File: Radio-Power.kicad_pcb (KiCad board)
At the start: 2 copper layers, 52.7 x 45.7 mm, 18 parts, among them J1 Input, J2 Radio Power, Q1 BS170, Q2 FQP27P06, Q3 BS170, U1 L7805, U2 ATtiny85-20PU

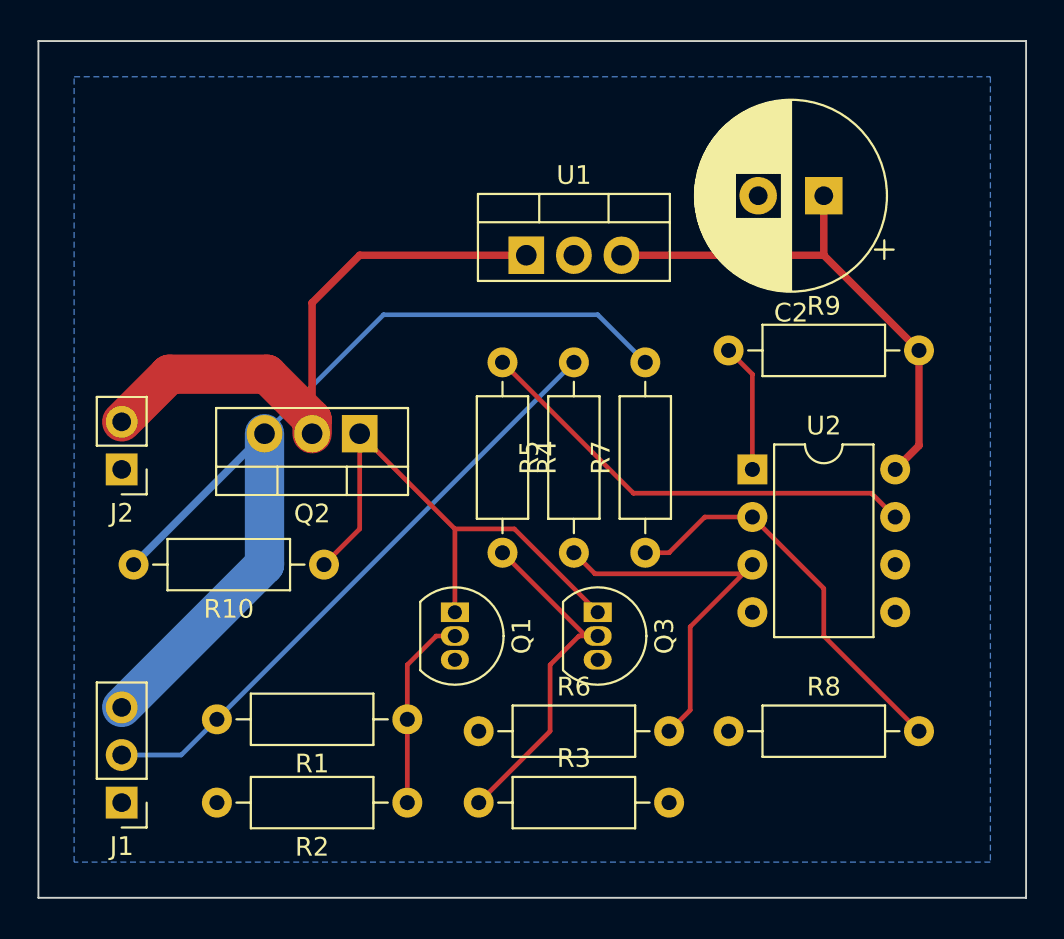
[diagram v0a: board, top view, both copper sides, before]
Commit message: Change some things, use switched power for measurement to prevent accidental power flow into the uC
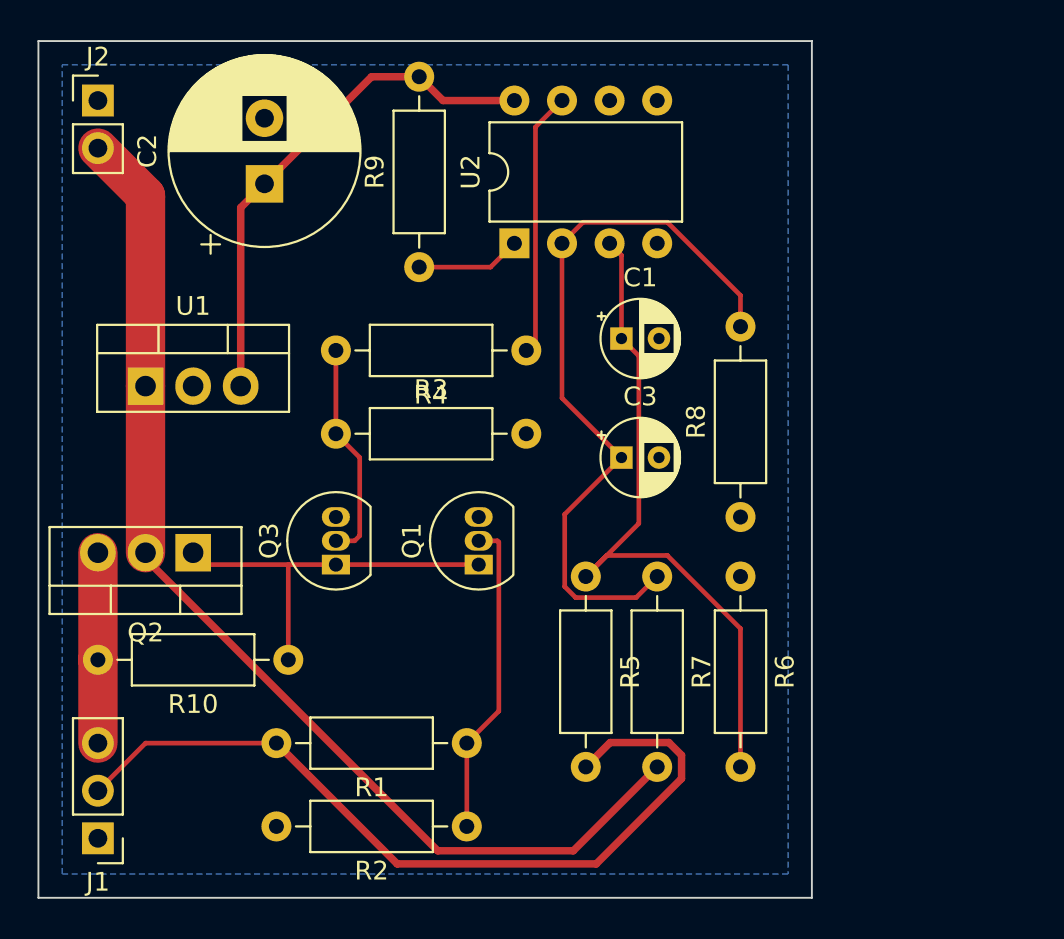
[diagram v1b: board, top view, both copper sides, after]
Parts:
- added C1: 1uF, Capacitor_THT:CP_Radial_D4.0mm_P2.00mm, F.Cu at (45.7, 30.5)
- added C3: 1uF, Capacitor_THT:CP_Radial_D4.0mm_P2.00mm, F.Cu at (45.7, 36.8)
- R5, R7: value 4.7K -> 47K
- R6, R8: value 1.5K -> 15K
- moved C2 29.9 mm to (26.7, 22.2), turned to 90 degrees
- moved U1 21.5 mm to (20.3, 33.0)
- moved R3 21.1 mm to (30.5, 35.6)
- moved J2 19.7 mm to (17.8, 17.8), turned to 0 degrees
- moved U2 17.5 mm to (40.0, 25.4), turned to 90 degrees
- moved R9 17.1 mm to (34.9, 26.7), turned to 90 degrees
- moved R6 16.2 mm to (52.1, 43.2), turned to 270 degrees
- moved Q3 14.2 mm to (30.5, 42.5), turned to 90 degrees
- moved R8 11.4 mm to (52.1, 40.0), turned to 90 degrees
- moved Q2 10.9 mm to (22.9, 41.9)
- moved R10 5.43 mm to (27.9, 47.6)
- moved R1 3.42 mm to (37.5, 52.1)
- moved R2 3.42 mm to (37.5, 56.5)
- moved Q1 2.84 mm to (38.1, 42.5), turned to 90 degrees
- moved J1 2.29 mm to (17.8, 57.1)
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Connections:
- R7 pad 2: Bat+ -> Switched
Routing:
- net Bat+: track 51.6 -> 10.2 mm
- net Switched: track 33.8 -> 58.6 mm
- net Net-(C3-Pad1): track 21.6 -> 39.8 mm
- net Net-(C1-Pad1): track 20.9 -> 37.3 mm
- net ACC: track 32.8 -> 43.9 mm
- net Net-(R4-Pad1): track 24.4 -> 14.1 mm
- net Net-(Q1-Pad1): track 28.9 -> 20.6 mm
- net Net-(Q3-Pad2): track 19.0 -> 11.8 mm
- net Net-(Q1-Pad2): track 10.5 -> 17.0 mm
- net Net-(R9-Pad1): track 6.88 -> 5.61 mm
- net GND: track 0.63 -> 0.00 mm
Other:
- board size 52.7 x 45.7 mm -> 41.3 x 45.7 mm

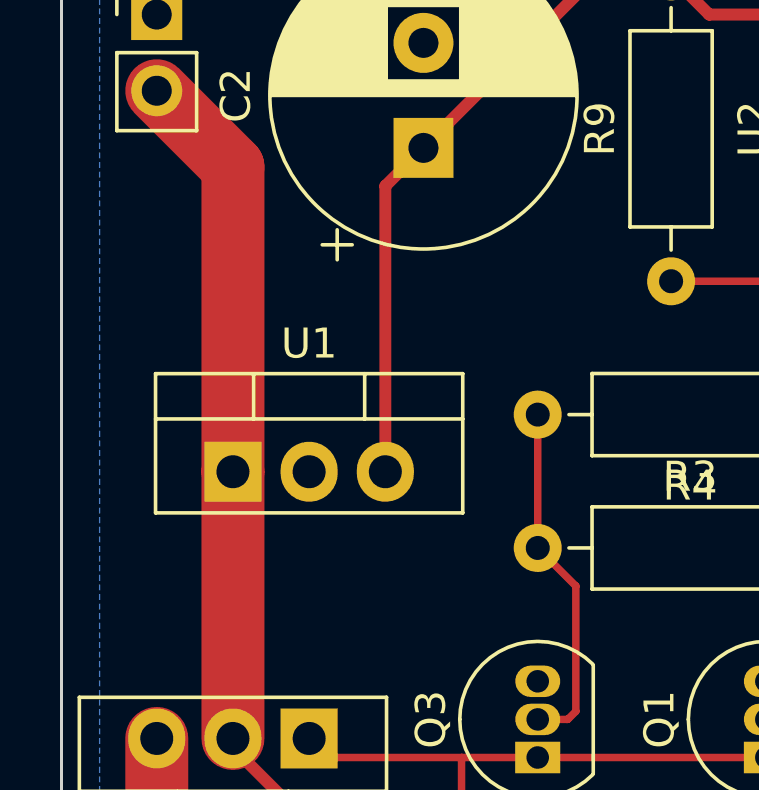
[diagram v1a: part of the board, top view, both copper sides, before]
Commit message: Board updated, switched to lm2936 for 5v regulator
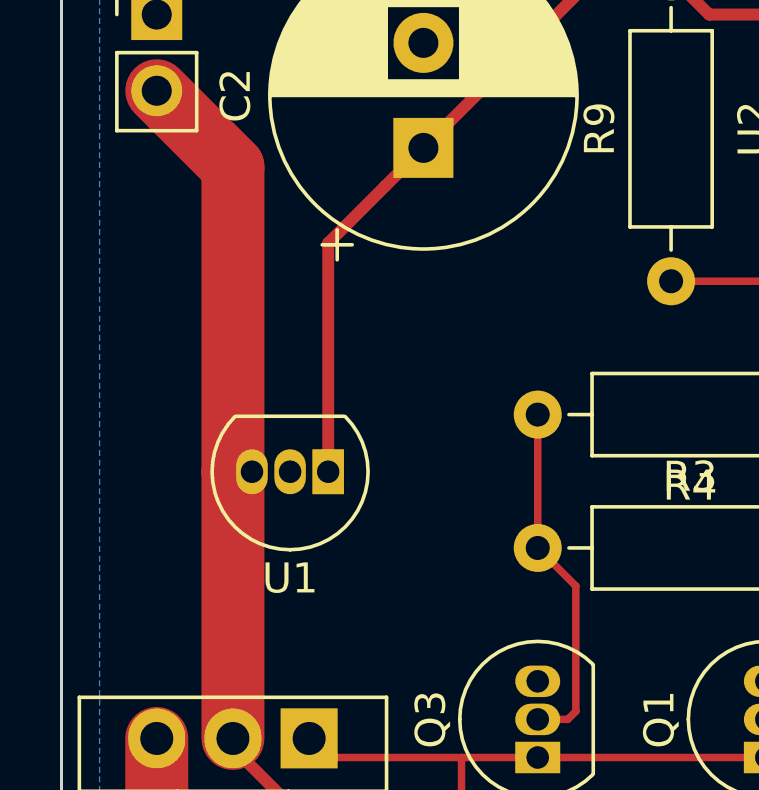
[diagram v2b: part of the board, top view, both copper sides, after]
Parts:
- U1: value L7805 -> LM2936-5.0_TO92; footprint Package_TO_SOT_THT:TO-220-3_Vertical -> Package_TO_SOT_THT:TO-92_Inline
- moved U1 3.18 mm to (23.5, 33.0), turned to 180 degrees
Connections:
- U1 pad 1: Switched -> 5V
- U1 pad 3: 5V -> Switched
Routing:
- net 5V: track 27.5 -> 28.3 mm

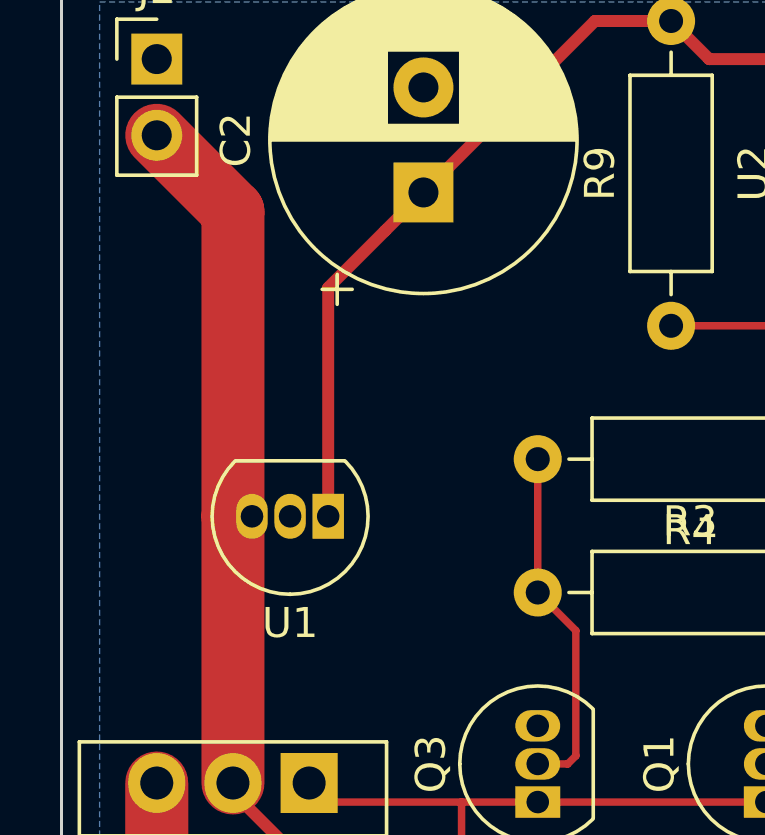
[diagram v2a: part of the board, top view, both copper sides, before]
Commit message: Minor updates, add a cap and move the regulator
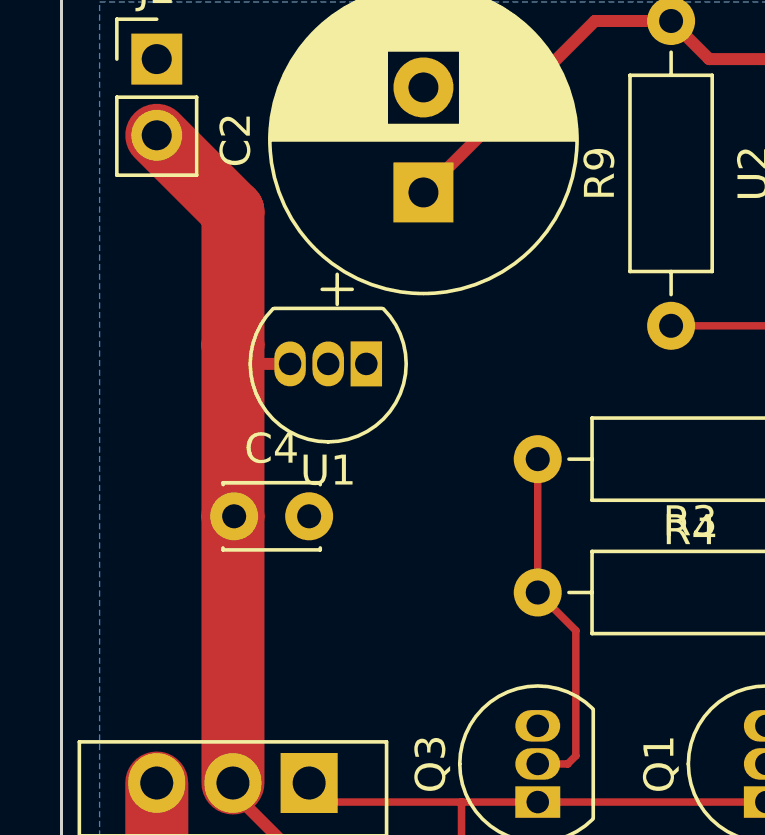
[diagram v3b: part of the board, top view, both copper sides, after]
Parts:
- added C4: 100nF, Capacitor_THT:C_Disc_D3.0mm_W2.0mm_P2.50mm, F.Cu at (20.4, 33.0)
- moved U1 5.24 mm to (24.8, 27.9)
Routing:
- net 5V: track 28.3 -> 16.2 mm
- net Switched: track 58.6 -> 60.7 mm
